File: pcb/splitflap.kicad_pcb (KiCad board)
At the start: 2 copper layers, 100 x 100 mm, 64 parts, among them J1 Motor D, J10 Hall C, J11 Hall B, J12 I2C, J2 Motor C, J3 Motor B, J4 Motor A, J5 BarrelJack Vertical, J6 USB_C_Receptacle_USB2.0_16P, J7 BarrelJack Horizontal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

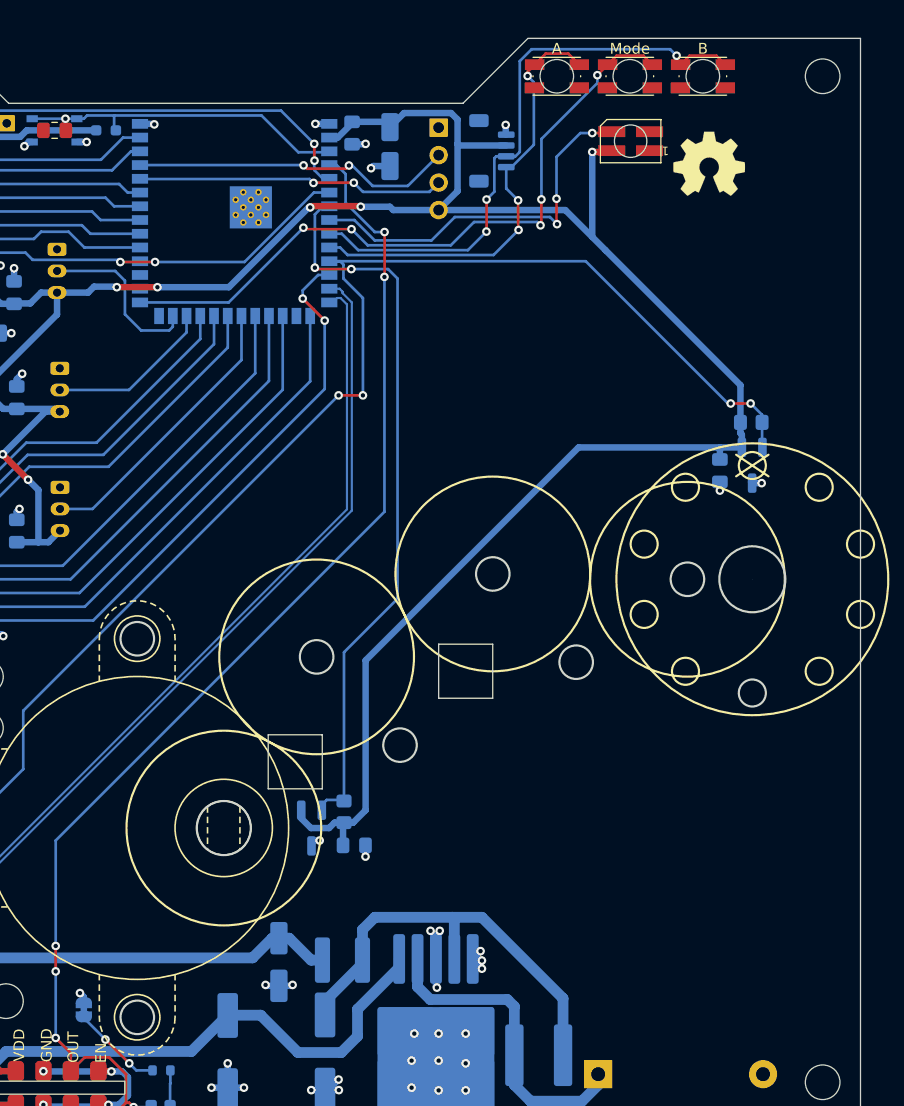
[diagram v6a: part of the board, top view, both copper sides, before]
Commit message: Add flap stop slot
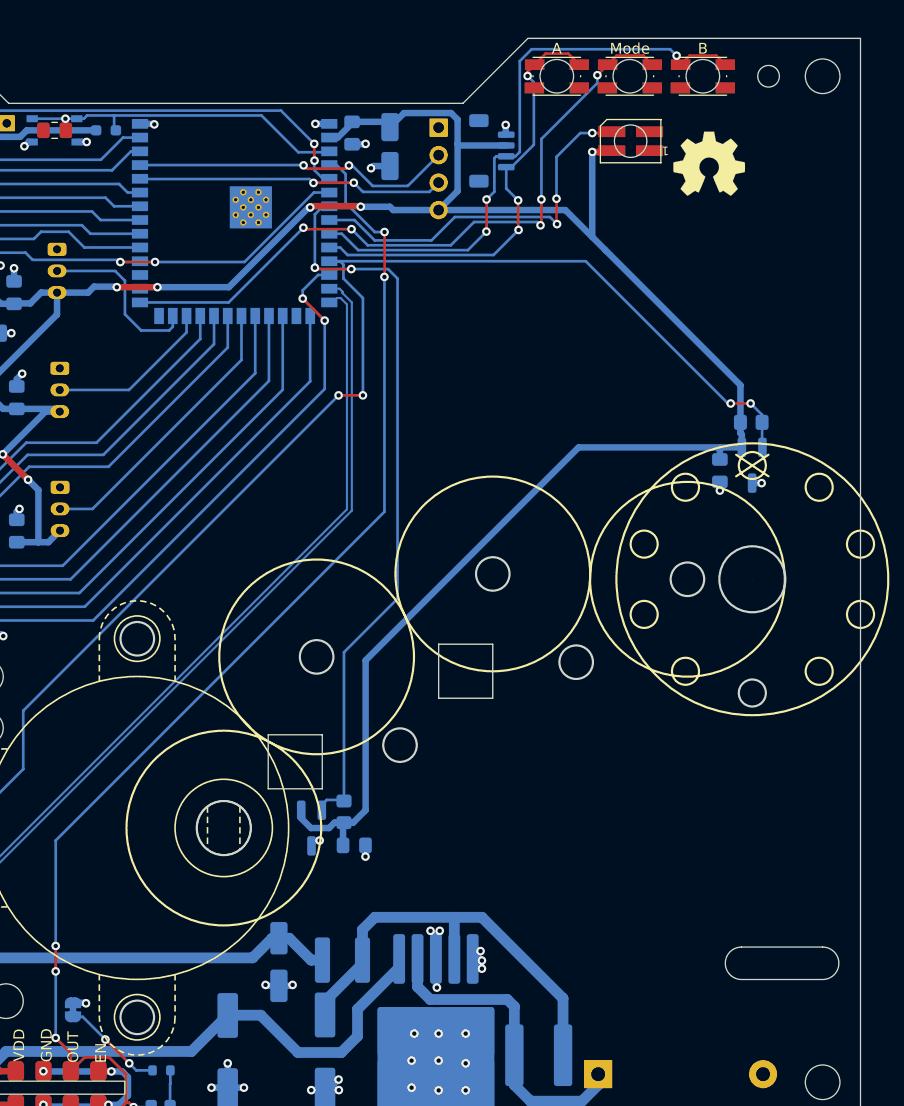
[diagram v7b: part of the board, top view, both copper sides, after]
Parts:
- moved JP2 1.00 mm to (127.2, 139.8)
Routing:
- net Net-(JP2-B): track 8.46 -> 9.40 mm
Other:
- outline, holes or cut-outs redrawn
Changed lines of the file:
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@@
 	(footprint "Jumper:SolderJumper-2_P1.3mm_Bridged_RoundedPad1.0x1.5mm"
 		(layer "B.Cu")
-		(at 128.2 139.8 -90)
+		(at 127.2 139.8 -90)
 		(descr "SMD Solder Jumper, 1x1.5mm, rounded Pads, 0.3mm gap, bridged with 1 copper strip")
 		(tags "net tie solder jumper bridged")
@@
 		)
 		(property "Value" "DCF77 LED"
-			(at 2.4 3 0)
+			(at 2.2 1.8 0)
 			(layer "B.SilkS")
 			(effects
@@
 		(tags "capacitor handsolder")
 		(property "Reference" "C17"
-			(at 0 1.68 360)
+			(at 0 1.68 0)
 			(layer "B.SilkS")
 			(hide yes)
@@
 		)
 		(property "Value" "100n"
-			(at 0 -1.68 360)
+			(at 0 -1.68 0)
 			(layer "B.Fab")
 			(effects
@@
 		)
 		(fp_text user "${REFERENCE}"
-			(at 0 0 360)
+			(at 0 0 0)
 			(layer "B.Fab")
 			(effects
@@
 	)
 	(gr_circle
+		(center 191.5 53.5)
+		(end 192.5 53.5)
+		(stroke
+			(width 0.1)
+			(type default)
+		)
+		(fill none)
+		(layer "Edge.Cuts")
+	)
+	(gr_circle
 		(center 166.006705 99.508732)
 		(end 167.556705 99.508732)
@@
 		(layer "Edge.Cuts")
 	)
+	(gr_line
+		(start 196.5 134)
+		(end 189 134)
+		(stroke
+			(width 0.1)
+			(type default)
+		)
+		(layer "Edge.Cuts")
+	)
 	(gr_circle
 		(center 190 110.514622)
@@
 		(layer "Edge.Cuts")
 	)
+	(gr_arc
+		(start 189 137)
+		(mid 187.5 135.5)
+		(end 189 134)
+		(stroke
+			(width 0.1)
+			(type default)
+		)
+		(layer "Edge.Cuts")
+	)
+	(gr_arc
+		(start 196.5 134)
+		(mid 198 135.5)
+		(end 196.5 137)
+		(stroke
+			(width 0.1)
+			(type default)
+		)
+		(layer "Edge.Cuts")
+	)
 	(gr_circle
 		(center 119.25 109)
@@
 		(layer "Edge.Cuts")
 	)
+	(gr_line
+		(start 196.5 137)
+		(end 189 137)
+		(stroke
+			(width 0.1)
+			(type default)
+		)
+		(layer "Edge.Cuts")
+	)
 	(segment
 		(start 107.25 116.5)
@@
 	)
 	(via
-		(at 127.842405 138.253273)
+		(at 128.4 139.2)
 		(size 0.8)
 		(drill 0.4)
@@
 	)
 	(segment
+		(start 128.4 139.2)
+		(end 128.35 139.15)
+		(width 0.6)
+		(layer "B.Cu")
+		(net 2)
+	)
+	(segment
 		(start 164.15 135.15)
 		(end 165 136)
@@
 	)
 	(segment
-		(start 128.2 138.610868)
-		(end 128.2 139.15)
-		(width 0.6)
-		(layer "B.Cu")
-		(net 2)
-	)
-	(segment
 		(start 113.05 74.75)
 		(end 113.55 75.25)
@@
 	)
 	(segment
-		(start 127.842405 138.253273)
-		(end 128.2 138.610868)
-		(width 0.6)
-		(layer "B.Cu")
-		(net 2)
-	)
-	(segment
 		(start 122 81.5)
 		(end 122.5 81)
@@
 	)
 	(segment
+		(start 128.35 139.15)
+		(end 127.2 139.15)
+		(width 0.6)
+		(layer "B.Cu")
+		(net 2)
+	)
+	(segment
 		(start 150.89 57.9)
 		(end 149.602 57.9)
@@
 	)
 	(segment
-		(start 134.55 145.4)
-		(end 133.05 145.4)
+		(start 130.2 142.55)
+		(end 128.1 140.45)
 		(width 0.25)
 		(layer "B.Cu")
@@
 	)
 	(segment
-		(start 128.2 140.55)
-		(end 128.2 140.45)
+		(start 134.55 145.4)
+		(end 133.05 145.4)
 		(width 0.25)
 		(layer "B.Cu")
@@
 	)
 	(segment
-		(start 130.2 142.55)
-		(end 128.2 140.55)
+		(start 128.1 140.45)
+		(end 127.2 140.45)
 		(width 0.25)
 		(layer "B.Cu")

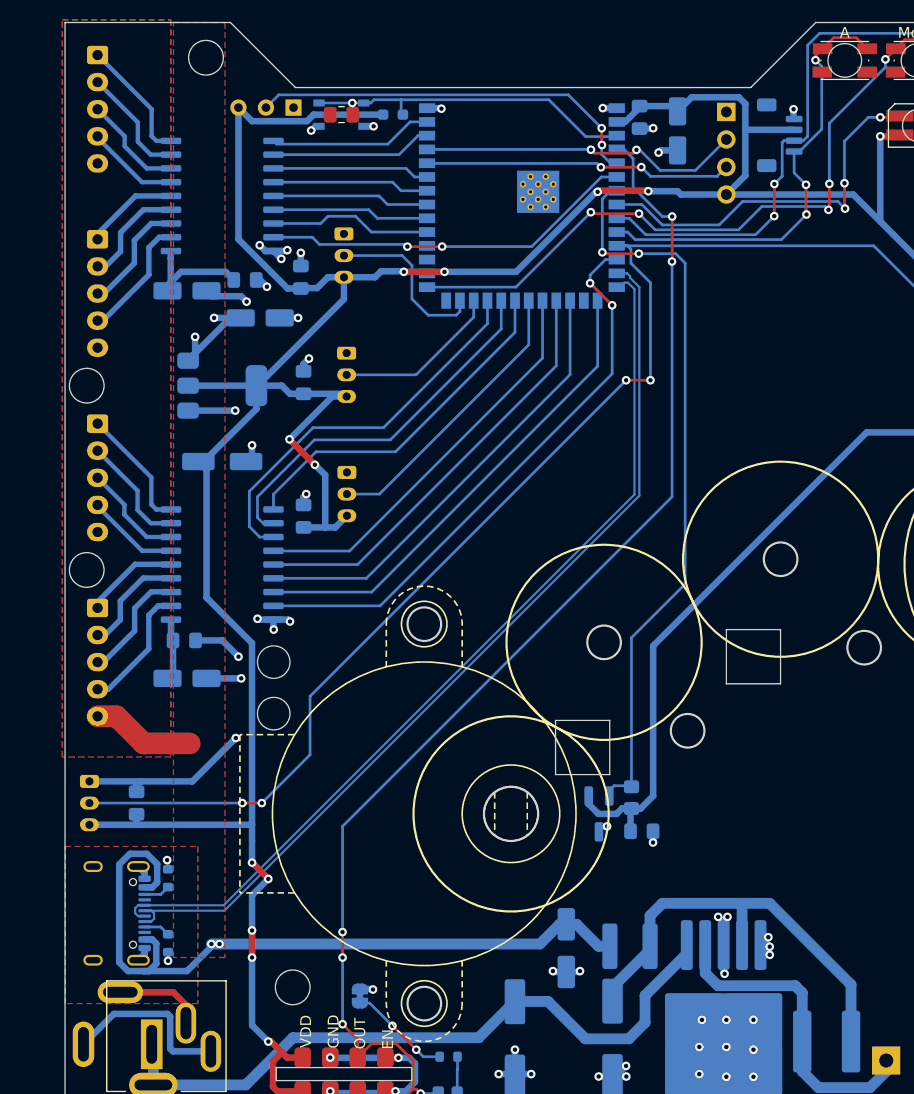
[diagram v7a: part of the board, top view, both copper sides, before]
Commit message: Add a PPTC fuse to the USB connection
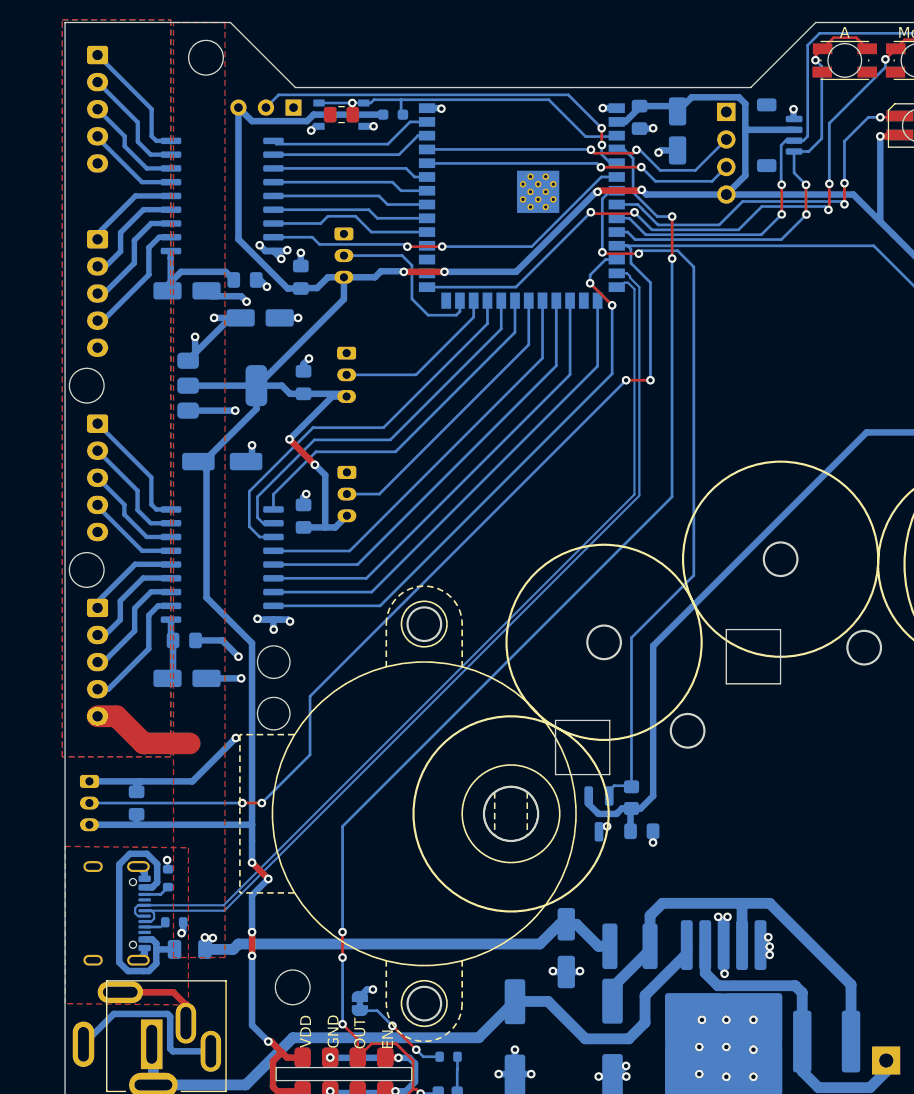
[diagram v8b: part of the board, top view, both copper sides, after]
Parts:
- added F1: PPTC, Fuse:Fuse_1206_3216Metric, B.Cu at (111.5, 135.5)
- moved R3 2.01 mm to (110.1, 133.0), turned to 0 degrees
- moved JP2 0.70 mm to (127.2, 140.5)
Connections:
- J6 pad A4: +5V -> Net-(F1-Pad1)
- J6 pad A9: +5V -> Net-(F1-Pad1)
- J6 pad B4: +5V -> Net-(F1-Pad1)
- J6 pad B9: +5V -> Net-(F1-Pad1)
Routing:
- net +5V: track 107.8 -> 80.2 mm
- net Net-(F1-Pad1): track 0.00 -> 25.2 mm
- net /HALL_A2: track 67.3 -> 68.4 mm
- net Net-(J6-CC1): track 2.44 -> 1.48 mm
- net Neopixel: track 35.3 -> 34.7 mm
- net /SWA_SCL: track 41.3 -> 41.8 mm
